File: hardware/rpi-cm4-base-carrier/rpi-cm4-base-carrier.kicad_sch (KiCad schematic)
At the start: 0 parts

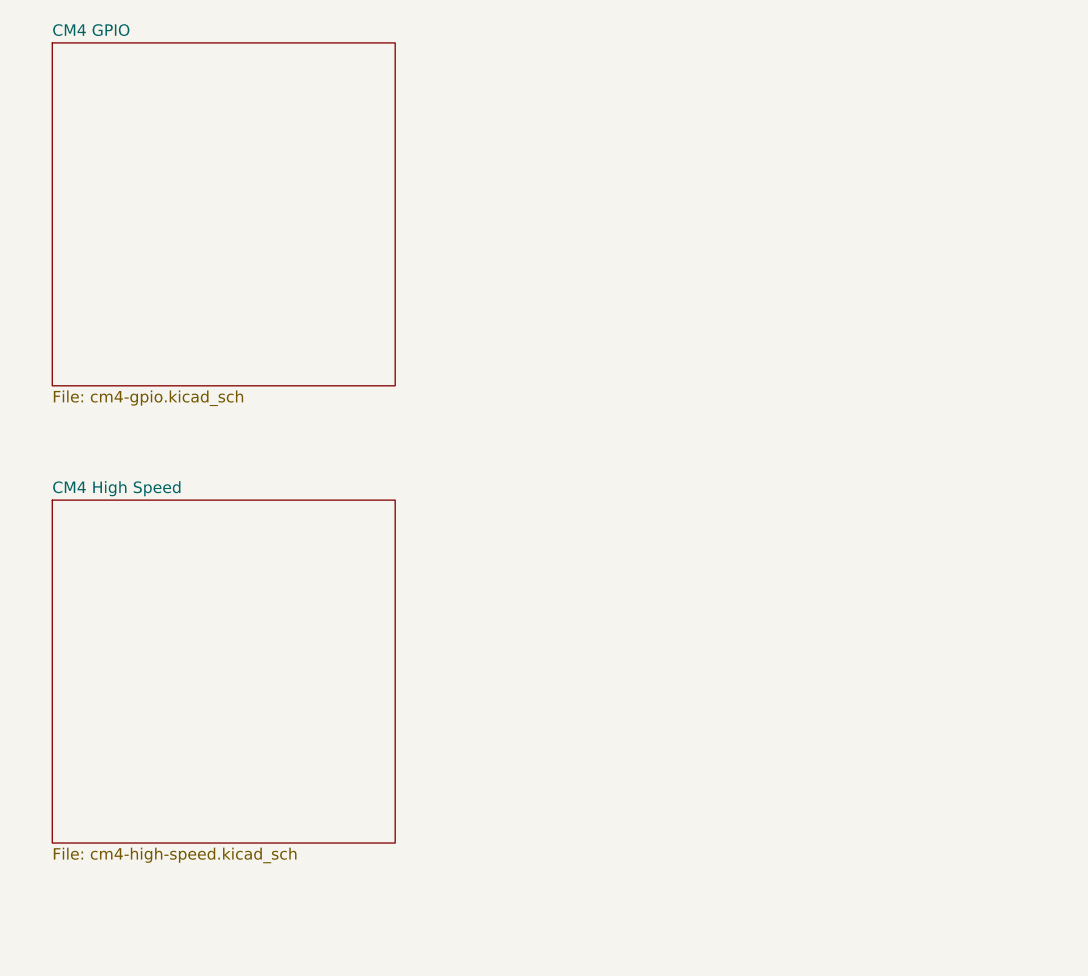
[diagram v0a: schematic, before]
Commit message: schematic changes to add network, hdmi, usbhost and SD
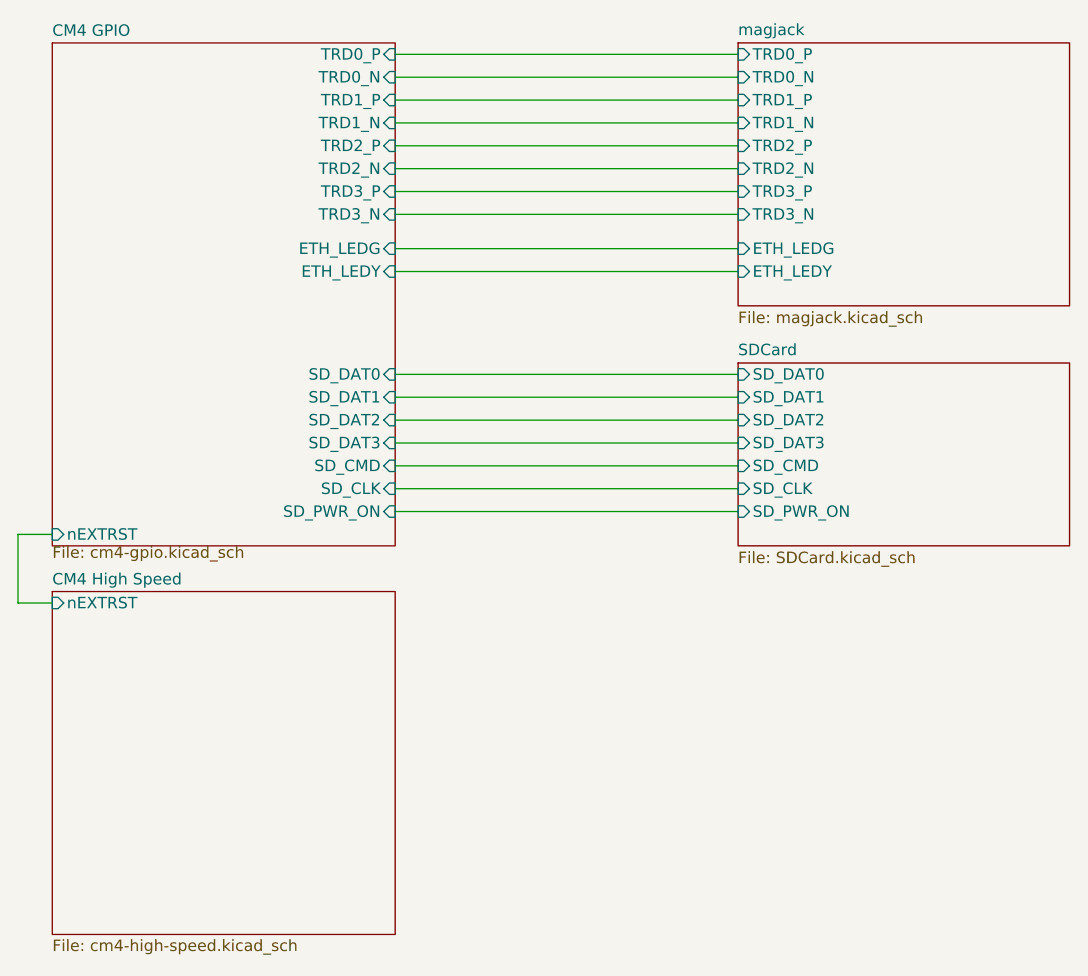
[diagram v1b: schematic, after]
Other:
- added sheet SDCard (SDCard.kicad_sch)
- added sheet magjack (magjack.kicad_sch)
- sheet CM4 GPIO ports: added ETH_LEDG, ETH_LEDY, SD_CLK, SD_CMD, SD_DAT0, SD_DAT1, SD_DAT2, SD_DAT3, SD_PWR_ON, TRD0_N, TRD0_P, TRD1_N, TRD1_P, TRD2_N, TRD2_P, TRD3_N, TRD3_P, nEXTRST; removed none
- sheet CM4 High Speed ports: added nEXTRST; removed none
